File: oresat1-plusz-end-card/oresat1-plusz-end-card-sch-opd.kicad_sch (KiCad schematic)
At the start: 58 parts, among them Q1 DMP2240UDM-7, Q11 DMP2240UDM-7, Q2 DMN3028LQ-7, Q3 DMN3028LQ-7, Q4 DMN3028LQ-7, Q6 DMN3028LQ-7, Q9 DMP2240UDM-7, U11 MIC842LYC5, U12 MIC842LYC5, U2 MAX7310, U201 TS5A21366, U202 TS5A21366, U203 TS5A21366, U204 TS5A21366

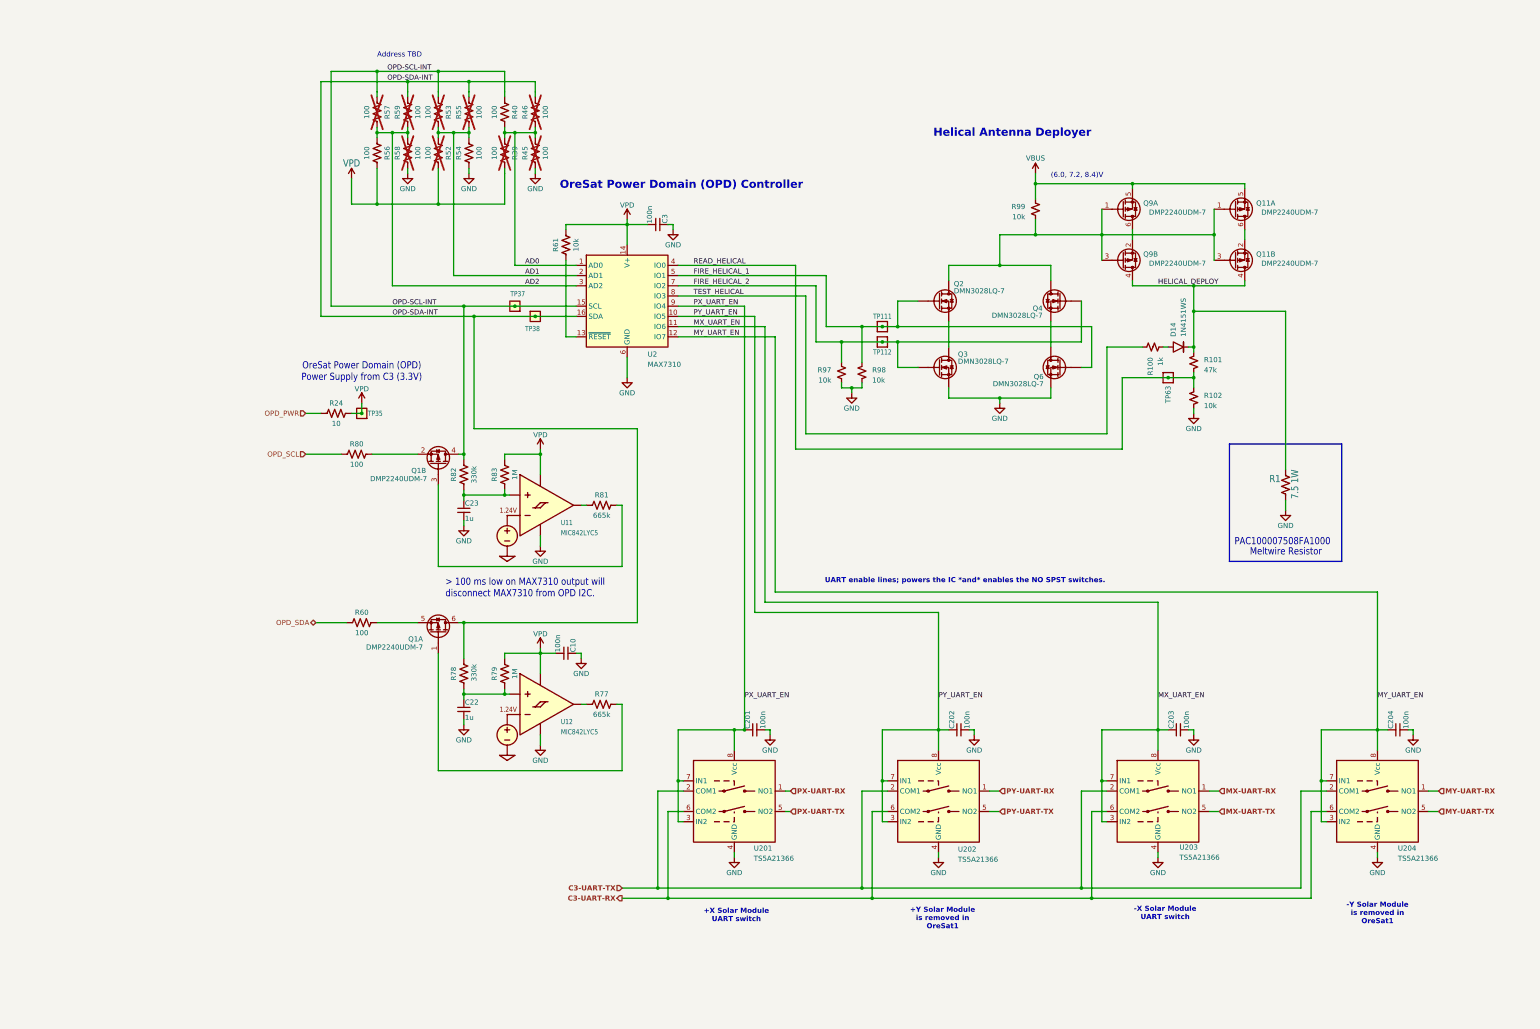
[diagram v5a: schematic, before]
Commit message: v1.1 sent to fab
Updated 3D models of connectors, added missing capacitors, fixed footprints, polished schematic, upgraded to single README file with Makefile.
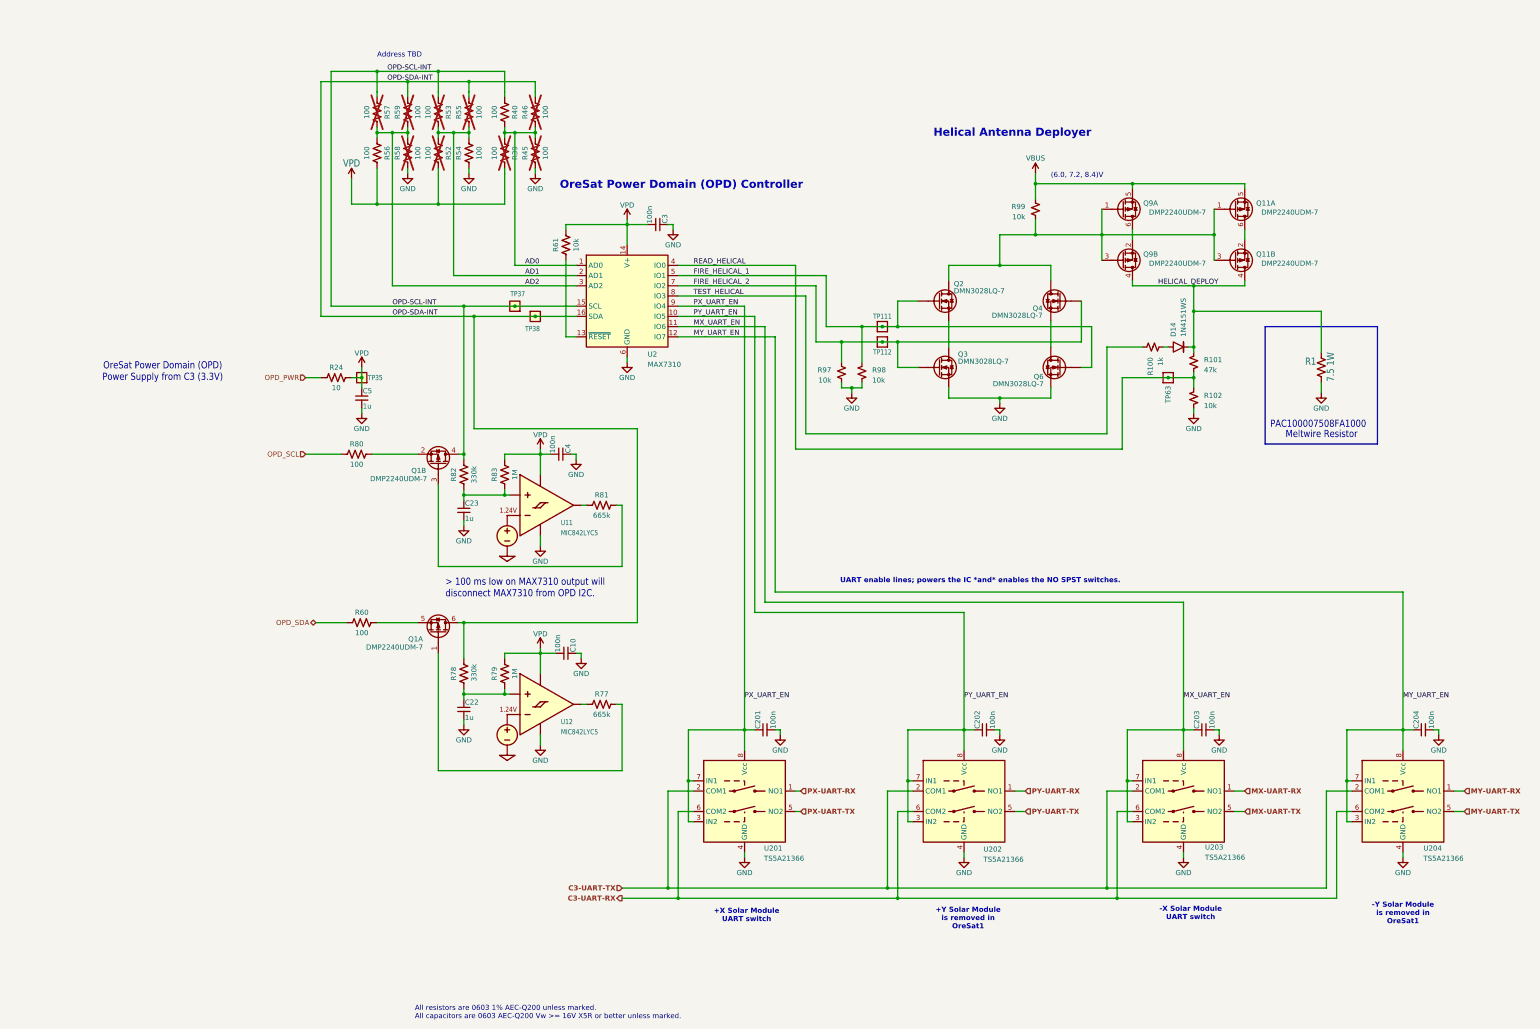
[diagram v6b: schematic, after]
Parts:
- added C4: 100n, oresat-passives:0603-C-NOSILK, symbol Device:C_Small
- added C5: 1u, oresat-passives:0603-C-NOSILK, symbol Device:C_Small
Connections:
- net GND: now also C4.1, C5.2
- net VPD: now also C4.2, C5.1
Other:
- note added: "All resistors are 0603 1% AEC-Q200 unless marked. All capacitors are 0603 AEC-Q200 Vw >= 16V X5R or better unless marked."
- moved on the sheet: C201, C202, C203, C204, R1, R24, TP35, U201, U202, U203, U204
